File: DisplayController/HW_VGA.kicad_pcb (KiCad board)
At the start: 2 copper layers, 150 x 90 mm, 77 parts, among them J1 Conn_02x40_Odd_Even, J301 Conn_01x02, J401 Conn_01x06, U102 GAL22V10, U103 74ALS163, U104 74ALS163, U105 74ALS163, U202 GAL22V10, U203 74ALS163, U204 74ALS163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

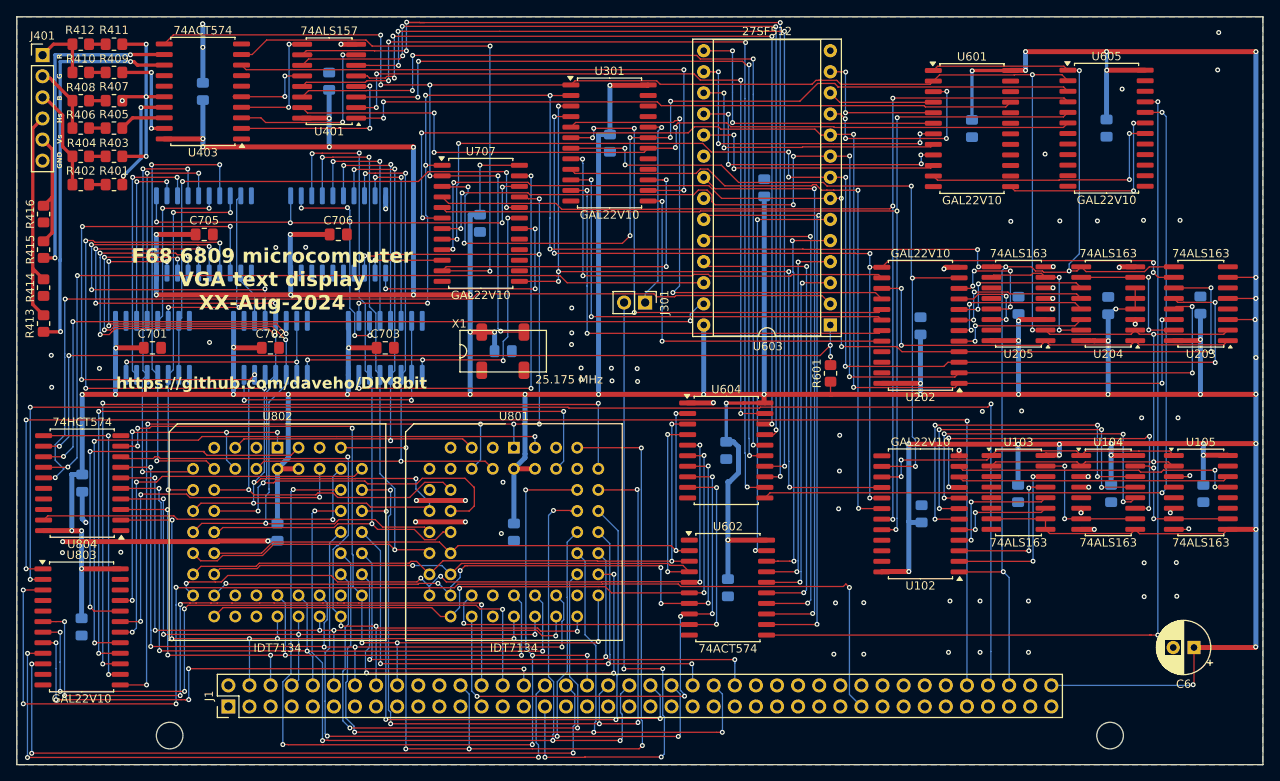
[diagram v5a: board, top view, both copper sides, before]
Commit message: fixed more unconnected ground plane fragments
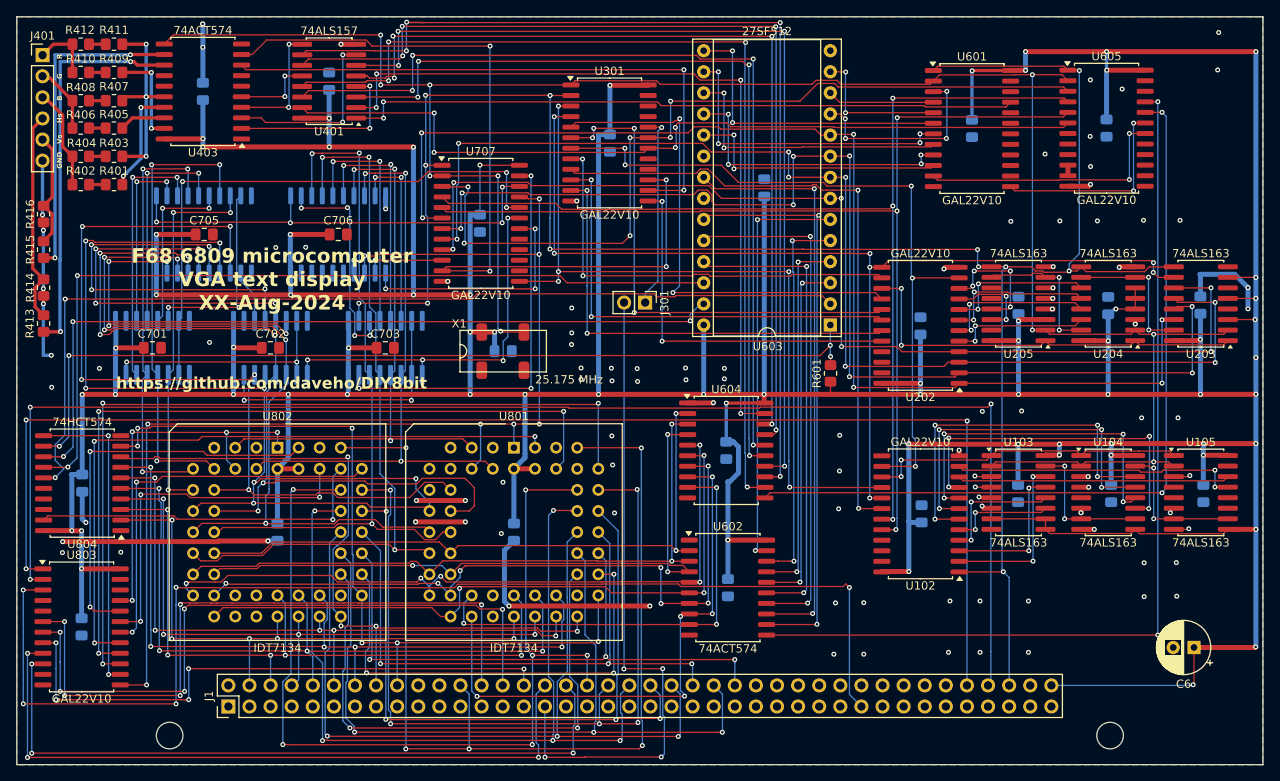
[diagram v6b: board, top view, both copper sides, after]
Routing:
- net GND: track 67.1 -> 141.1 mm, vias 76 -> 102
- net /Output/HSyncOut: track 26.6 -> 25.6 mm
- net /Output/VSyncOut: track 14.7 -> 14.0 mm
- net /Output/Intense: vias 4 -> 3

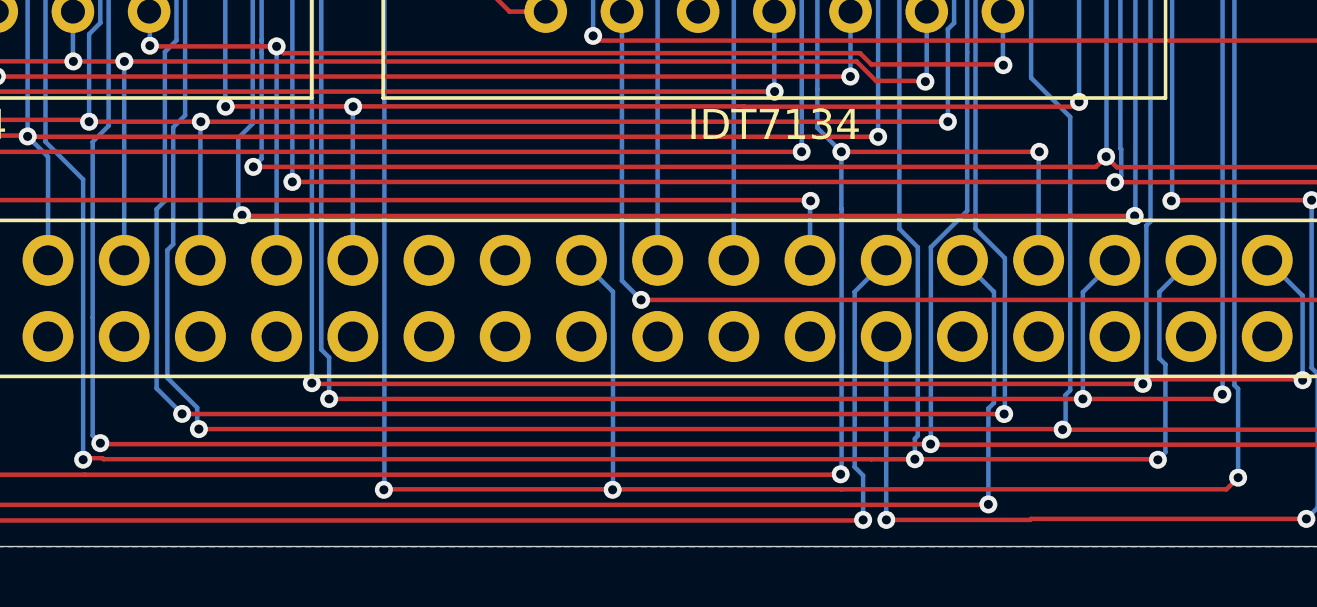
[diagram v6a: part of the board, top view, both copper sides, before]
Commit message: fixed a couple of unconnected host address lines
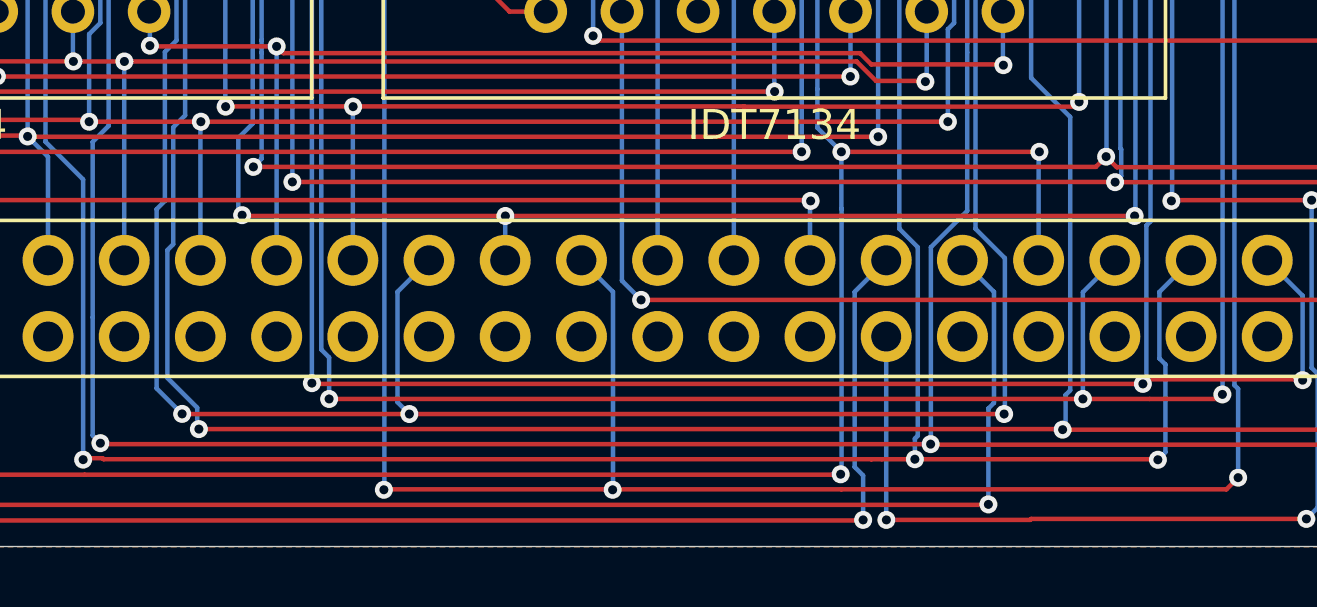
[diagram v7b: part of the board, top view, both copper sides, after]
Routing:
- net /HostA8: track 66.2 -> 71.9 mm, vias 2 -> 3
- net /HostA9: track 56.1 -> 57.5 mm, vias 3 -> 4
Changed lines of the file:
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@@
 	(segment
 		(start 131 144.004)
+		(end 111.175 144.004)
+		(width 0.15)
+		(layer "F.Cu")
+		(net 57)
+	)
+	(segment
+		(start 111.175 144.004)
 		(end 103.604 144.004)
 		(width 0.15)
@@
 	)
 	(via
+		(at 111.175 144.004)
+		(size 0.6)
+		(drill 0.3)
+		(layers "F.Cu" "B.Cu")
+		(net 57)
+	)
+	(via
 		(at 131 144.004)
 		(size 0.6)
@@
 		(drill 0.3)
 		(layers "F.Cu" "B.Cu")
+		(net 57)
+	)
+	(segment
+		(start 110.778 143.607)
+		(end 111.175 144.004)
+		(width 0.15)
+		(layer "B.Cu")
 		(net 57)
 	)
@@
 	)
 	(segment
+		(start 111.83 138.88)
+		(end 110.778 139.932)
+		(width 0.15)
+		(layer "B.Cu")
+		(net 57)
+	)
+	(segment
+		(start 110.778 139.932)
+		(end 110.778 143.607)
+		(width 0.15)
+		(layer "B.Cu")
+		(net 57)
+	)
+	(segment
 		(start 103.6 144)
 		(end 102.75 143.15)
@@
 	(segment
 		(start 135.35 137.402)
-		(end 105.627 137.402)
+		(end 114.375 137.402)
 		(width 0.15)
 		(layer "F.Cu")
@@
 		(net 69)
 	)
+	(segment
+		(start 114.375 137.402)
+		(end 105.627 137.402)
+		(width 0.15)
+		(layer "F.Cu")
+		(net 69)
+	)
 	(via
 		(at 135.35 137.402)
@@
 	(via
 		(at 105.6 137.375)
+		(size 0.6)
+		(drill 0.3)
+		(layers "F.Cu" "B.Cu")
+		(net 69)
+	)
+	(via
+		(at 114.375 137.402)
 		(size 0.6)
 		(drill 0.3)
@@
 	)
 	(segment
+		(start 114.37 138.88)
+		(end 114.37 137.407)
+		(width 0.15)
+		(layer "B.Cu")
+		(net 69)
+	)
+	(segment
 		(start 105.9532 126.4232)
 		(end 105.04 125.51)
@@
 		(width 0.15)
 		(layer "B.Cu")
+		(net 69)
+	)
+	(segment
+		(start 114.37 137.407)
+		(end 114.375 137.402)
+		(width 0.15)
+		(layer "B.Cu")
